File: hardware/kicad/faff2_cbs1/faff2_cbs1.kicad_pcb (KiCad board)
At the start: 4 copper layers, 210 x 130 mm, 412 parts, among them J1001 USB_C_Receptacle_USB2.0_16P, J1002 TSW-105-07-F-D, J1003 SAMTEC_SHF-107-01-L-D-SM, J1101 1x6 2.54mm, J1102 1x6 2.54mm, J1103 Micro-Fit 1x3, J201 KPJX-4S, J301 PH1-06-UA, J501 1729076, J502 8510-4500PL, J503 CONUFL001-SMD, J504 CONUFL001-SMD, J601 FH12-10S-0.5SH(55), J602 FTSH-105-01-L-DV-K-TR, J603 8510-4500PL, J701 1752120, J702 1752120, J703 8510-4500PL, J901 BTN EXT, J902 SMA Jack, J903 J-LIM, Q1101 BSZ099N06LS5, Q1102 BSZ099N06LS5, Q1103 BSZ099N06LS5, Q1104 BSZ099N06LS5, Q1105 BSZ099N06LS5, Q1106 BSZ099N06LS5, Q201 DMP6023LFG-7, SW1001 PTS526, SW901 PTS526, SW902 PTS526, SW903 PTS526, SW904 PTS526, U1001 STM32H723VET6, U1002 USB3320C, U1003 SRAM 32Mb, U1004 MIC5365-1.8, U1101 DRV8323S, U301 LMR33630, U302 ADPL42005, U303 ADPL42005, U304 LMR33630, U501 ADS1235, U601 AM26LV32, U701 ADS1120, U801 24FC16T-I/OT, U901 SN74LVC1G17, U902 SN74LVC1G11, Y1001 24MHz, Y1002 24MHz 18pF

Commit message: pcb: round 2 step 1 - restack to six layers, JLC06161H-7628
The captain's round-2 ruling authorises two more internal layers for power:
SIG / GND / PWR / PWR / GND / SIG.  House G1's substance is preserved rather
than waived -- G1 exists so every signal is plane-referenced, and every
outer-layer signal still faces an unbroken ground plane 0.2104 mm below it,
the same reference distance the 4-layer build gave.  What changes is that
power no longer has to share the signal layers.

The stackup is JLC's published template, not a guess: JLC06161H-7628, 6-layer
1.6 mm at 1 oz outer / 0.5 oz inner, the same no-surcharge class and the same
Nan Ya NP-155F materials as the 4-layer board.

Choosing -7628 from JLC's ten 6-layer options is the whole point.  Its outer
prepreg is identical to the 4-layer board's -- 7628, 0.2104 mm, Dk 4.40 -- so
every impedance number already derived carries over untouched: the USB pair
stays 0.30/0.20 for 90.6 ohm and SYNC stays 0.37 for 50 ohm, and round 1's
hand-drawn pair does not have to be redrawn.  Every alternative (-1080 at
0.0764, -3313 at 0.0994, -2116 at 0.1164/0.1270) moves the reference plane
closer and would have forced both geometries to narrow.

Board 1.582 mm including mask.  The second ground plane moved In2.Cu ->
In4.Cu.  Zones refilled; DRC still zero real violations, parity 0, unconnected
unchanged at 111.

Co-Authored-By: Claude Opus 5 <noreply@anthropic.com>
Claude-Session: https://claude.ai/code/session_01WqUrajr7x5bwUMvjXpVkdq
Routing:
- added copper zone on In4.Cu, net GND
- removed copper zone on In2.Cu, net GND
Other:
- copper layers 4 -> 6
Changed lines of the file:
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@@
 	(generator_version "9.0")
 	(general
-		(thickness 1.6062)
+		(thickness 1.582)
 		(legacy_teardrops no)
 	)
@@
 		(0 "F.Cu" mixed)
 		(4 "In1.Cu" power "GND Plane L2")
-		(6 "In2.Cu" power "GND Plane L3")
+		(6 "In2.Cu" power "PWR Plane L3")
+		(8 "In3.Cu" power "PWR Plane L4")
+		(10 "In4.Cu" power "GND Plane L5")
 		(2 "B.Cu" mixed)
 		(9 "F.Adhes" user "F.Adhesive")
@@
 			(layer "dielectric 2"
 				(type "core")
-				(thickness 1.065)
+				(thickness 0.4)
 				(material "NP-155F Core")
-				(epsilon_r 4.43)
+				(epsilon_r 4.36)
 				(loss_tangent 0.02)
 			)
@@
 				(loss_tangent 0.02)
 			)
+			(layer "In3.Cu"
+				(type "copper")
+				(thickness 0.0152)
+			)
+			(layer "dielectric 4"
+				(type "core")
+				(thickness 0.4)
+				(material "NP-155F Core")
+				(epsilon_r 4.36)
+				(loss_tangent 0.02)
+			)
+			(layer "In4.Cu"
+				(type "copper")
+				(thickness 0.0152)
+			)
+			(layer "dielectric 5"
+				(type "prepreg")
+				(thickness 0.2104)
+				(material "NP-155F 7628")
+				(epsilon_r 4.4)
+				(loss_tangent 0.02)
+			)
 			(layer "B.Cu"
 				(type "copper")
@@
 		(net 118)
 		(net_name "GND")
-		(layer "In2.Cu")
+		(layer "In4.Cu")
 		(hatch edge 0.5)
 		(connect_pads

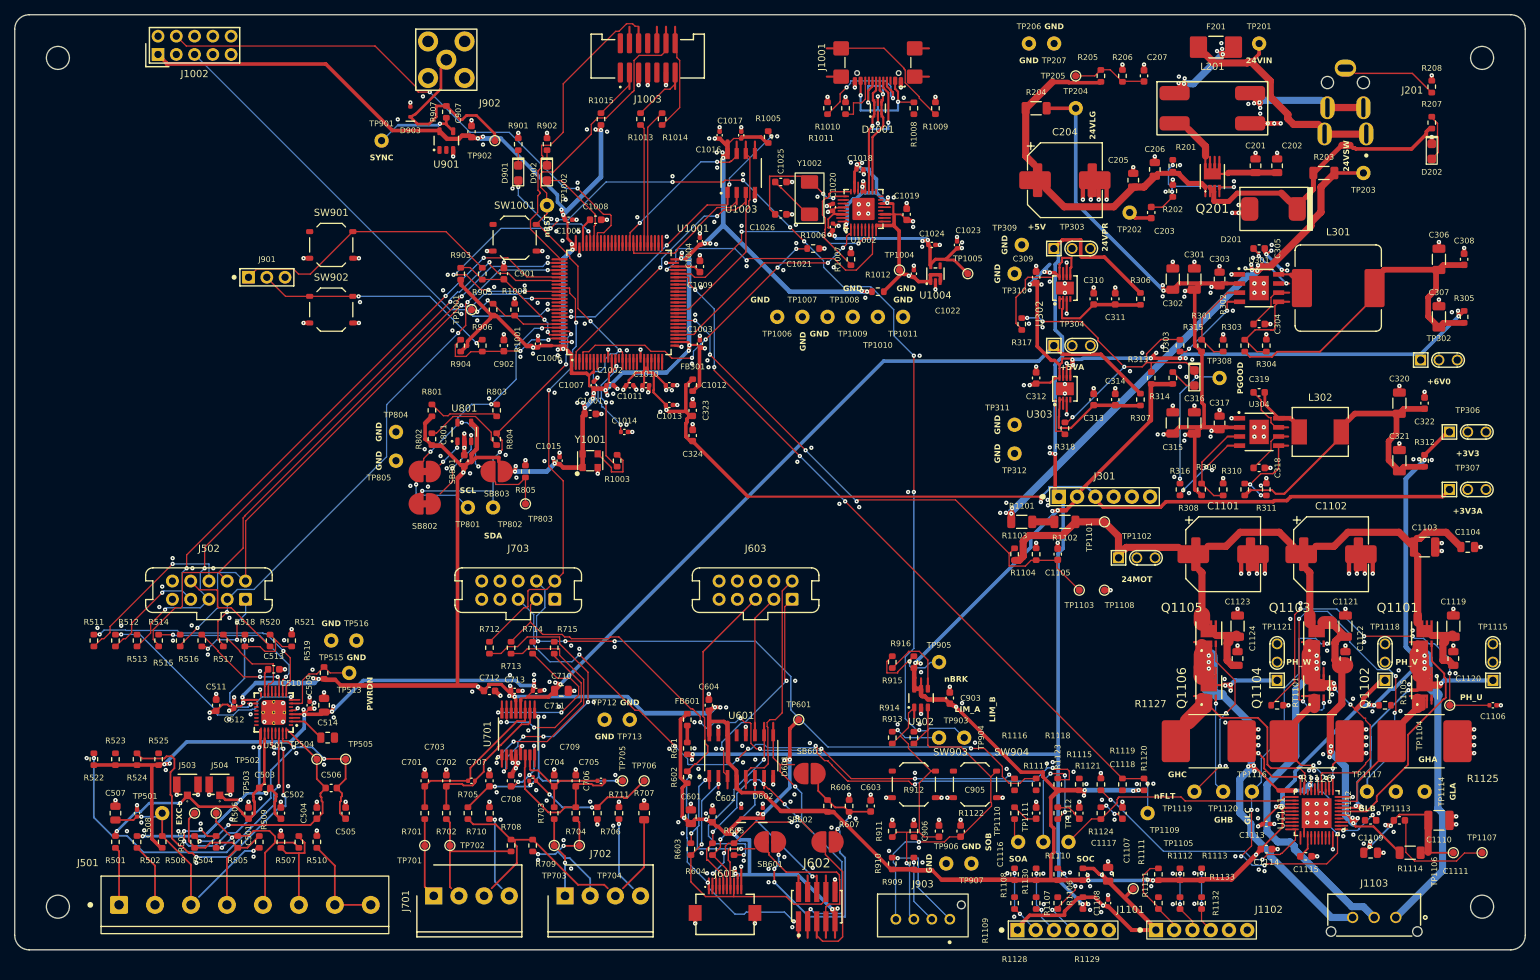
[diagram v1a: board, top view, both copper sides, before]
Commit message: pcb: round 2 step 2 - take the movable power rails off the signal layers
1703 mm of outer copper freed, 23 % of every trace on the board: 7471 -> 5768.
+3V3 alone was 715 mm of it.  Unconnected rises 111 -> 271, which is the point:
those thirteen rails are deliberately unrouted now and get rebuilt on In2/In3
in step 4.

Which nets move is set by what 0.5 oz internal copper will carry, not by
preference.  IPC-2221 for an internal conductor is I = 0.024 dT^0.44 A^0.725
against 0.048 external -- half the constant -- and JLC's inner foil is
0.0152 mm against 0.035 outside.  At the 10 degC rise the rest of this board
is sized to, 0.5 mm carries 0.40 A, 2.0 mm carries 1.08 A and 6.0 mm carries
2.39 A.  A 3 A net would want roughly 8 mm of internal width.

So the 3 A nets stay outer -- the 24 V entry chain, V24_MOT, the three phases
and the three low-side source nets -- where 1 oz gives 2.39 A at 1.00 mm and
they are already drawn and proved against the via budget.  The two buck SW
nodes stay outer as well, and would even at microamps: threading a
discontinuous-current node through two vias into a buried layer is the
opposite of what the house rules and both datasheets ask.

One bug worth the note: the rip matched nothing on its first run because the
net list was JSON-encoded twice, so the child interpreter built a set of
single characters and no net ever matched.  It reported "ripped 0" cheerfully.

Co-Authored-By: Claude Opus 5 <noreply@anthropic.com>
Claude-Session: https://claude.ai/code/session_01WqUrajr7x5bwUMvjXpVkdq
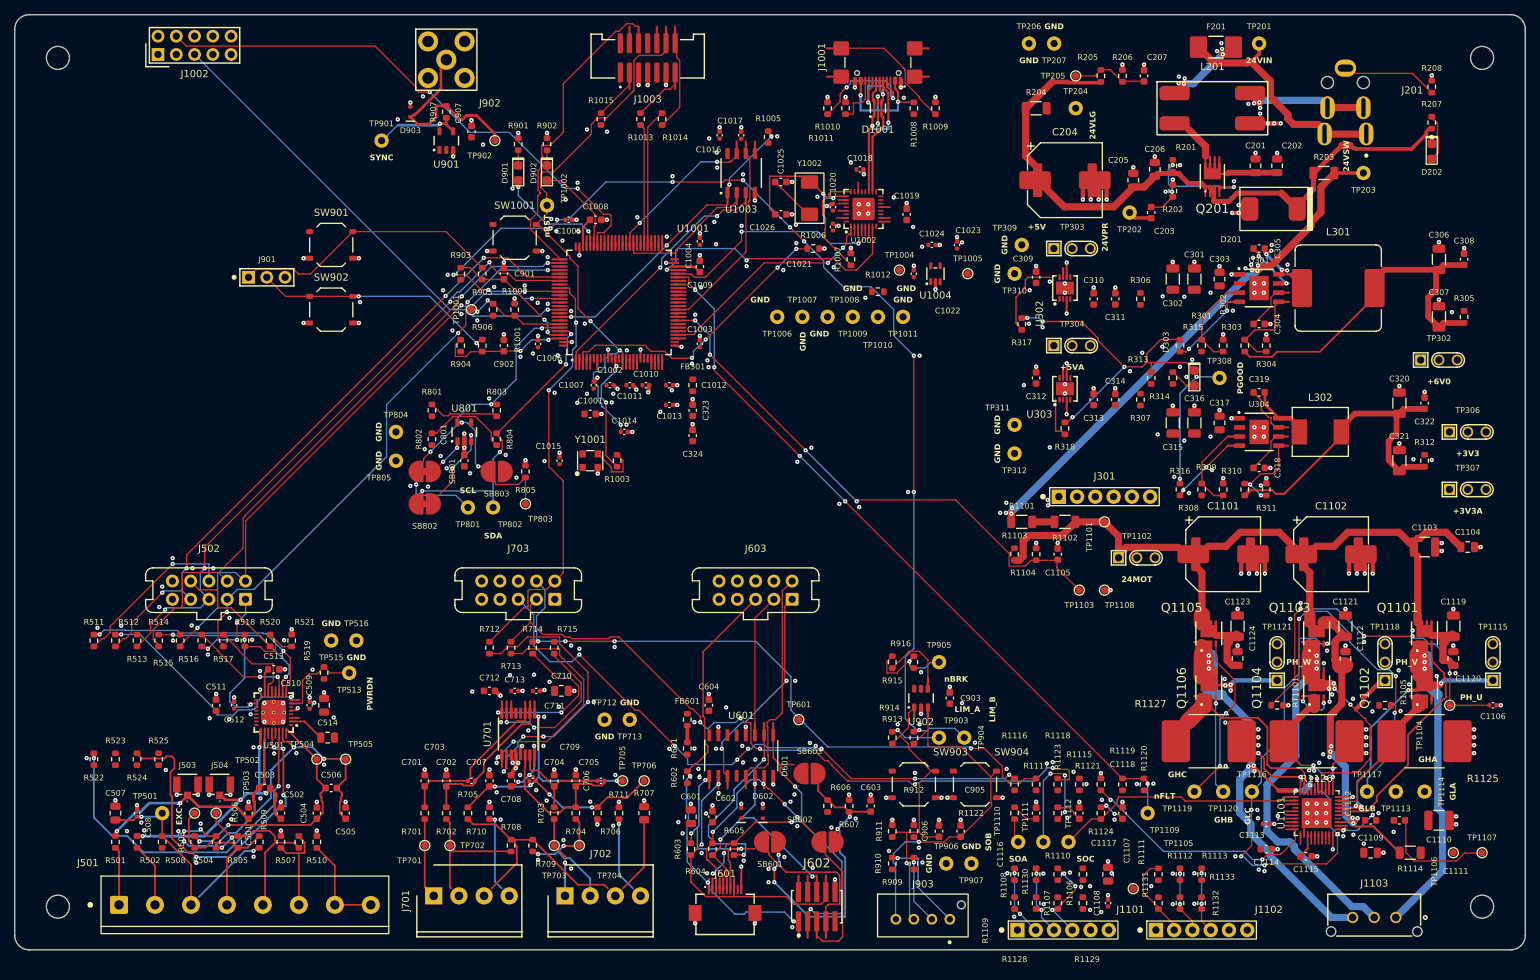
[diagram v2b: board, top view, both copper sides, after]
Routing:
- net +3V3: track 715.5 -> 0.00 mm, vias 67 -> 0
- net +5VA: track 201.8 -> 0.00 mm, vias 11 -> 0
- net +5V: track 167.8 -> 0.00 mm, vias 6 -> 0
- net +3V3A: track 145.6 -> 0.00 mm, vias 6 -> 0
- net /power_rails/+6V0: track 106.6 -> 0.00 mm, vias 13 -> 0
- net /power_entry_24v/V24_LOGIC: track 92.5 -> 0.00 mm, vias 7 -> 0
- net /linear_encoder/+5V_ENC: track 80.1 -> 0.00 mm, vias 12 -> 0
- net /mcu/+3V3_USB: track 60.4 -> 0.00 mm, vias 10 -> 0
- net /mcu/+1V8_USB: track 38.5 -> 0.00 mm, vias 6 -> 0
- net /motor_drive/VENC: track 37.7 -> 0.00 mm, vias 2 -> 0
- net /motor_drive/VM_DRV: track 22.2 -> 0.00 mm, vias 4 -> 0
- net Net-(U303-SENSE): track 18.0 -> 0.00 mm
- net Net-(U302-SENSE): track 15.9 -> 0.00 mm

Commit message: pcb: round 2 step 3 - signal fill pass 1 on the freed corridors
78 -> 63 open signal nets, unconnected 271 -> 253.  The rate is what the
freed copper bought: five nets per twelve-net chunk against round 1's one,
on the same nets the same stage could not touch before.

route6_signals skips the thirteen rails that now live on In2/In3 -- without
that it would put +3V3 straight back on F.Cu, which is the copper step 2
just cleared.

Co-Authored-By: Claude Opus 5 <noreply@anthropic.com>
Claude-Session: https://claude.ai/code/session_01WqUrajr7x5bwUMvjXpVkdq
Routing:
- net /mcu/MOTOR_ENCODER_I: track 1.50 -> 123.5 mm, vias 0 -> 2
- net /mcu/HALL1: track 1.50 -> 122.5 mm, vias 0 -> 4
- net /mcu/V24_MON: track 11.7 -> 95.9 mm, vias 0 -> 2
- net /mcu/SPARE_PC13: track 1.50 -> 79.4 mm, vias 0 -> 4
- net /mcu/LIMIT_nBRK: track 14.3 -> 73.2 mm
- net /mcu/ULPI_DIR: track 2.80 -> 61.3 mm, vias 0 -> 2
- net /linear_encoder/ENC_SDO: track 3.85 -> 55.2 mm, vias 0 -> 3
- net Net-(U1101-SOA): track 4.62 -> 53.1 mm, vias 0 -> 4
- net /mcu/SYNC_TRIG: track 1.50 -> 47.4 mm, vias 0 -> 2
- net /mcu/ULPI_D6: track 2.80 -> 44.6 mm, vias 0 -> 4
- net Net-(U1101-SDI): track 1.34 -> 42.4 mm, vias 0 -> 2
- net /mcu/ULPI_D5: track 2.80 -> 43.4 mm, vias 0 -> 4
- net +3V3: track 0.00 -> 23.0 mm
- net /temp_sense/ADS1120_nDRDY: track 1.65 -> 24.3 mm, vias 0 -> 1
- net Net-(U501B-AIN3): track 1.20 -> 22.1 mm, vias 0 -> 2
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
